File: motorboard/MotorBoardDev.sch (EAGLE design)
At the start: 71 parts, among them J1 Under Glow, J2 Safety Light, J3 12V, J4 24V, T1 NCP1117DT50GOS-ND, T3 NCP1117DT33GOS-ND, U1 TXB0104DR, U2 9DoF IMU, U3 TXB0104DR, U4 TXB0104DR, X1 C-GRID-05-15-91, X2 C-GRID-05-15-91, X3 MINI-USB_SHIELD5P4-32005-400, X4 C-GRID-02-70553, X5 SI-50170, X7 2510-, X8 2510-

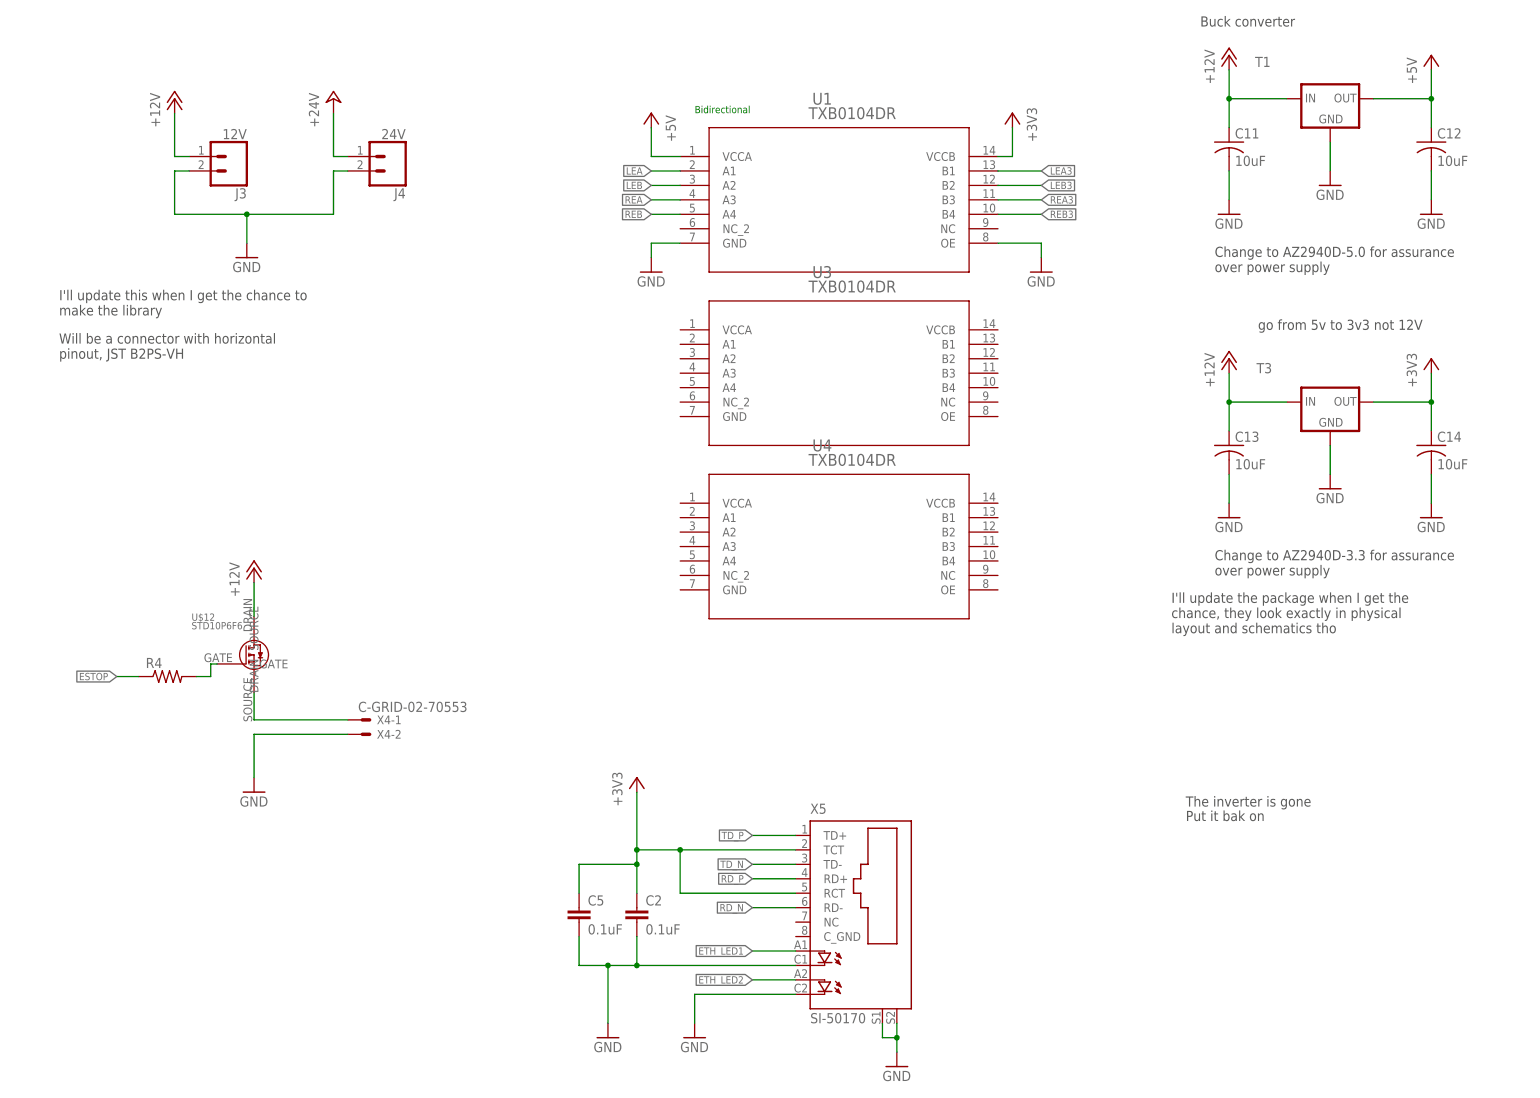
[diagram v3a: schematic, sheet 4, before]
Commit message: Motor board updated after design review
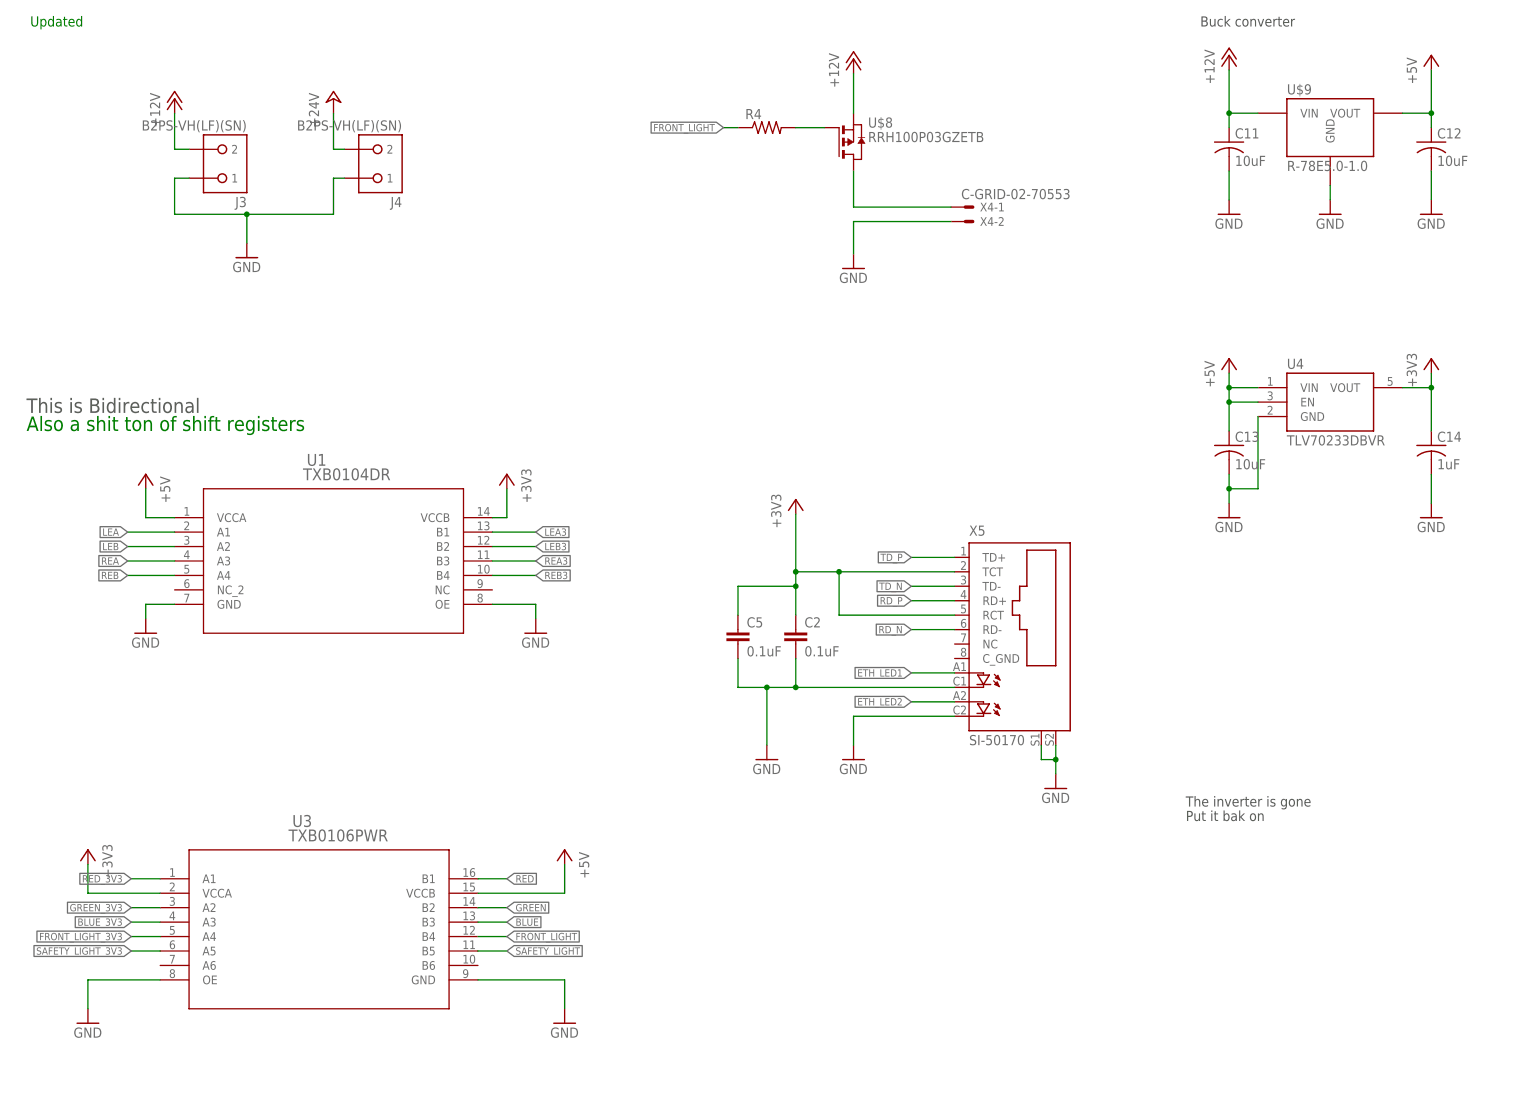
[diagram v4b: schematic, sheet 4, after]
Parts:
- removed R11, R12, R13, R14, R15, R6: 200, SparkFun-Resistors:200OHM-0603-1/10W-1%
- removed T1: NCP1117DT50GOS-ND, IGVC-Regulators:NCP1117DT50GOS-ND
- removed T3: NCP1117DT33GOS-ND, IGVC-Regulators:NCP1117DT33GOS-ND
- removed U$10, U$11, U$12: STD10P6F6, MotorBoardDev:STD10P6F6
- added Q1, Q2, Q3: SSM3J338R, RoboJackets-Discrete:PMOS
- added Q4: STT4P3LLH6, MotorBoardDev:STT4P3LLH6
- C14: value 10uF -> 1uF
- J2: value Safety Light -> B2PS-VH(LF)(SN); device SparkFun-Retired:CONN_02POLAR -> RoboJackets-Connectors:B2PS-VH(LF)(SN)
- J3: value 12V -> B2PS-VH(LF)(SN); device SparkFun-Connectors:CONN_025MM -> RoboJackets-Connectors:B2PS-VH(LF)(SN)
- J4: value 24V -> B2PS-VH(LF)(SN); device SparkFun-Connectors:CONN_025MM -> RoboJackets-Connectors:B2PS-VH(LF)(SN)
- U$8: value STD10P6F6 -> RRH100P03GZETB; device MotorBoardDev:STD10P6F6 -> MotorBoardDev:RRH100P03GZETB
- U$9: value STD10P6F6 -> R-78E5.0-1.0; device MotorBoardDev:STD10P6F6 -> MotorBoardDev:R-78E5.0-1.0
- U3: value TXB0104DR -> TXB0106PWR; device MotorBoardDev:TXB0104DR -> MotorBoardDev:TXB0106PWR
- U4: value TXB0104DR -> TLV70233DBVR; device MotorBoardDev:TXB0104DR -> RoboJackets-PowerICs:TLV70233DBVR
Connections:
- removed net 1S1: A1.P$18, R6.1
- removed net 1S1O: J1.4
- removed net 1S2: A1.P$17, R12.1
- removed net 1S2O: J1.5
- removed net 1S3: A1.P$16, R14.1
- removed net 1S3O: J1.6
- removed net 2S1: A1.P$7, R11.1
- removed net 2S1O: J1.10
- removed net 2S2: A1.P$6, R13.1
- removed net 2S2O: J1.11
- removed net 2S3: A1.P$5, R15.1
- removed net 2S3O: J1.12
- removed net ESTOP: A1.P$27, R4.1
- removed net N$11: R14.2
- removed net N$13: R12.2
- removed net N$14: R6.2
- removed net N$15: R11.2
- removed net N$16: R13.2
- removed net N$28: R15.2
- removed net N$3: R1.2, U$8.GATE
- new net BLUE_3V3: A1.P$29, U3.A3
- new net FRONT_LIGHT: R4.1, U3.B4
- new net FRONT_LIGHT_3V3: A1.P$27, U3.A4
- new net GREEN_3V3: A1.P$28, U3.A2
- new net N$26: Q1.G, R1.2
- new net RED_3V3: A1.P$30, U3.A1
- new net SAFETY_LIGHT_3V3: A1.P$19, U3.A5
- net +12V: now also J3.2, Q1.S, Q2.S, Q3.S, Q4.S, U$8.S, U$9.VIN; no longer C13.1, J3.1, T1.IN, T3.IN, U$10.DRAIN, U$11.DRAIN, U$12.DRAIN, U$8.DRAIN, U$9.DRAIN
- net +24V: now also J4.2; no longer J4.1
- net +3V3: now also U3.VCCA, U4.VOUT; no longer T3.OUT
- net +5V: now also C13.1, U$9.VOUT, U3.VCCB, U4.EN, U4.VIN; no longer T1.OUT
- net BLUE: now also U3.B3; no longer A1.P$29
- net BLUE_OUT: now also Q3.D; no longer U$10.SOURCE
- net GND: now also J1.10, J1.11, J1.12, J1.4, J1.5, J1.6, J3.1, J4.1, U$9.GND, U4.GND; no longer J2.2, J3.2, J4.2, T1.GND, T3.GND
- net GREEN: now also U3.B2; no longer A1.P$28
- net GREEN_OUT: now also Q2.D; no longer U$9.SOURCE
- net N$1: now also J2.2, Q4.D; no longer J2.1, U$11.SOURCE
- net N$10: now also U$8.D; no longer U$12.SOURCE
- net N$19: now also Q2.G; no longer U$9.GATE
- net N$4: now also Q3.G; no longer U$10.GATE
- net N$7: now also Q4.G; no longer U$11.GATE
- net N$8: now also U$8.G; no longer U$12.GATE
- net RED: now also U3.B1; no longer A1.P$30
- net RED_OUT: now also Q1.D; no longer U$8.SOURCE
- net SAFETY_LIGHT: now also U3.B5; no longer A1.P$19
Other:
- note added: "Also a shit ton of shift registers"
- note added: "Review the connection of DISABLE even tho it physically works"
- note added: "This is Bidirectional"
- note added: "This is the gigantic Yellow light on the top power rating as 1.2A average, 3A peak. Transistor here can take 4A"
- note added: "Updated"
- note removed: "Bidirectional"
- note removed: "Change to AZ2940D-3.3 for assurance over power supply"
- note removed: "Change to AZ2940D-5.0 for assurance over power supply"
- note removed: "I'll update the package when I get the chance, they look exactly in physical layout and schematics tho"
- note removed: "I'll update this when I get the chance to make the library"
- note removed: "Review the connection of DISABLE"
- note removed: "This transistor will be FQP27P06 as well"
- note removed: "Will be a connector with horizontal pinout, JST B2PS-VH"
- note removed: "go from 5v to 3v3 not 12V"
- moved on the sheet: C2, C5, J2, J4, R1, R2, R3, R30, R4, U1, X4-1, X4-2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

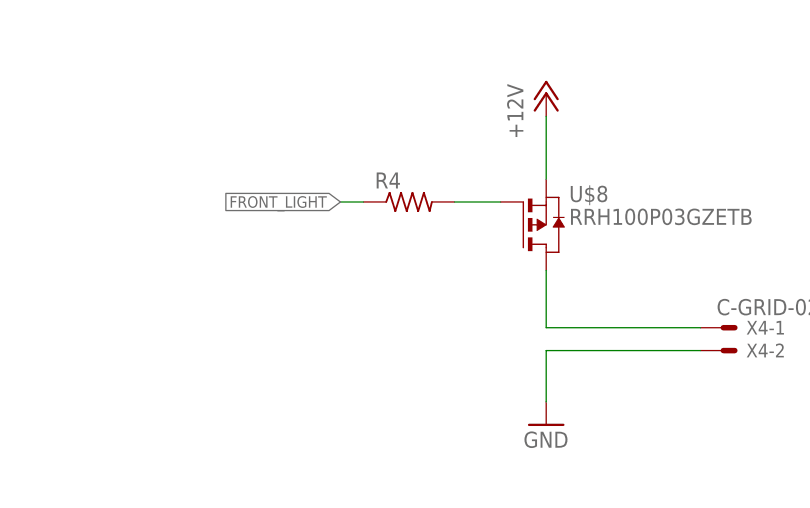
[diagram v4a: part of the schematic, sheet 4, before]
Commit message: added value to R4
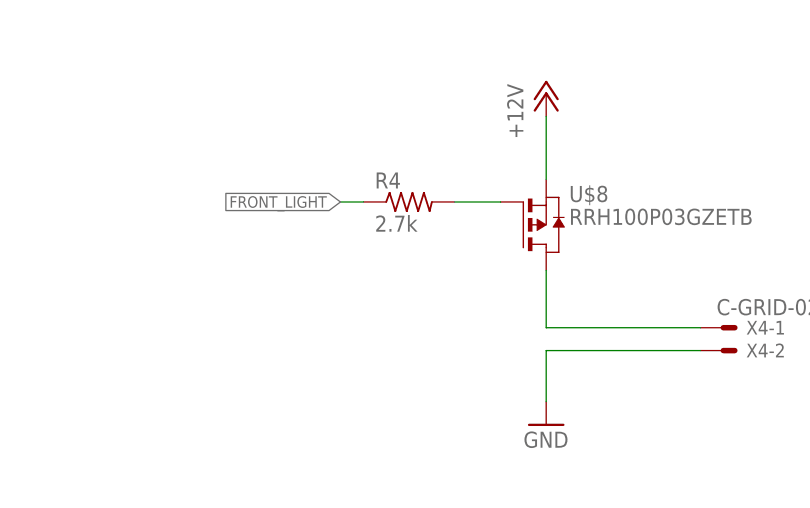
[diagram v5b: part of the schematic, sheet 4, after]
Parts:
- R4: value (none) -> 2.7k
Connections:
- net GND: now also J2.1
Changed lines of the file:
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@@
 <part name="U$7" library="IGVC-Power" deviceset="RGND" device=""/>
 <part name="R30" library="SparkFun-Resistors" deviceset="3.9KOHM" device="-0603-1/10W-1%" value="2700"/>
-<part name="R4" library="rcl" library_urn="urn:adsk.eagle:library:334" deviceset="R-US_" device="R0603" package3d_urn="urn:adsk.eagle:package:23555/2"/>
+<part name="R4" library="rcl" library_urn="urn:adsk.eagle:library:334" deviceset="R-US_" device="R0603" package3d_urn="urn:adsk.eagle:package:23555/2" value="2.7k"/>
 <part name="+3V5" library="supply1" deviceset="+3V3" device=""/>
 <part name="P+6" library="supply1" deviceset="+5V" device=""/>
@@
 <wire x1="226.06" y1="83.82" x2="226.06" y2="86.36" width="0.1524" layer="91"/>
 <wire x1="241.3" y1="86.36" x2="226.06" y2="86.36" width="0.1524" layer="91"/>
-</segment>
-<segment>
+<pinref part="J2" gate="G$1" pin="1"/>
+</segment>
+<segment>
